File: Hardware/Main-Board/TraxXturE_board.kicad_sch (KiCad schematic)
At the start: 0 parts

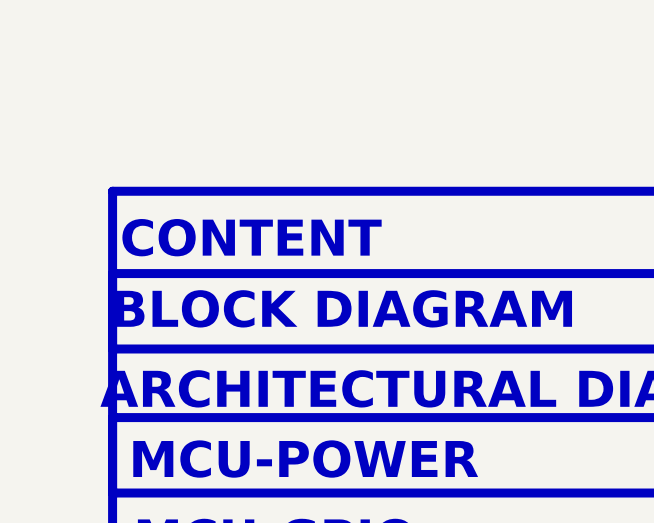
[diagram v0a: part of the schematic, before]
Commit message: Done with main board design, and camera interconnect in progress
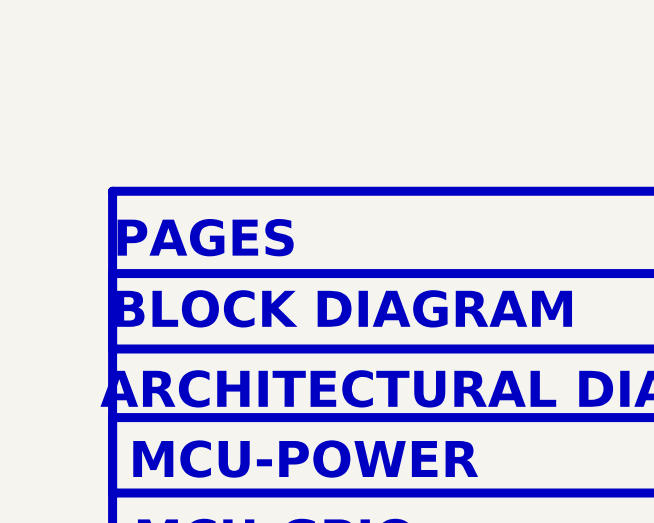
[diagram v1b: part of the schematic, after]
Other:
- note added: "PAGES"
- note removed: "CONTENT"
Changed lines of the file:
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@@
 		(comment 1 "1.0")
 		(comment 2 "Hassan  Omotoba")
+		(comment 3 "DRAFT")
 	)
 	(polyline
@@
 	)
 	(image
-		(at 221.234 129.54)
+		(at 221.488 88.9)
 		(scale 0.182963)
 		(data "iVBORw0KGgoAAAANSUhEUgAAB4AAAAQ4CAYAAADo08FDAAAANmVYSWZNTQAqAAAAGAAAAEgAAAAB"
@@
 		)
 	)
-	(text "CONTENT"
+	(text "PAGES"
 		(exclude_from_sim no)
-		(at 29.21 38.1 0)
+		(at 24.13 38.1 0)
 		(effects
 			(font
